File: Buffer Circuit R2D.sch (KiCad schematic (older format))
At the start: 25 parts, among them Q13 BC846B, Q14 BC856B, Q15 BC846B, Q16 BC856B, U10 AD8664ARZ

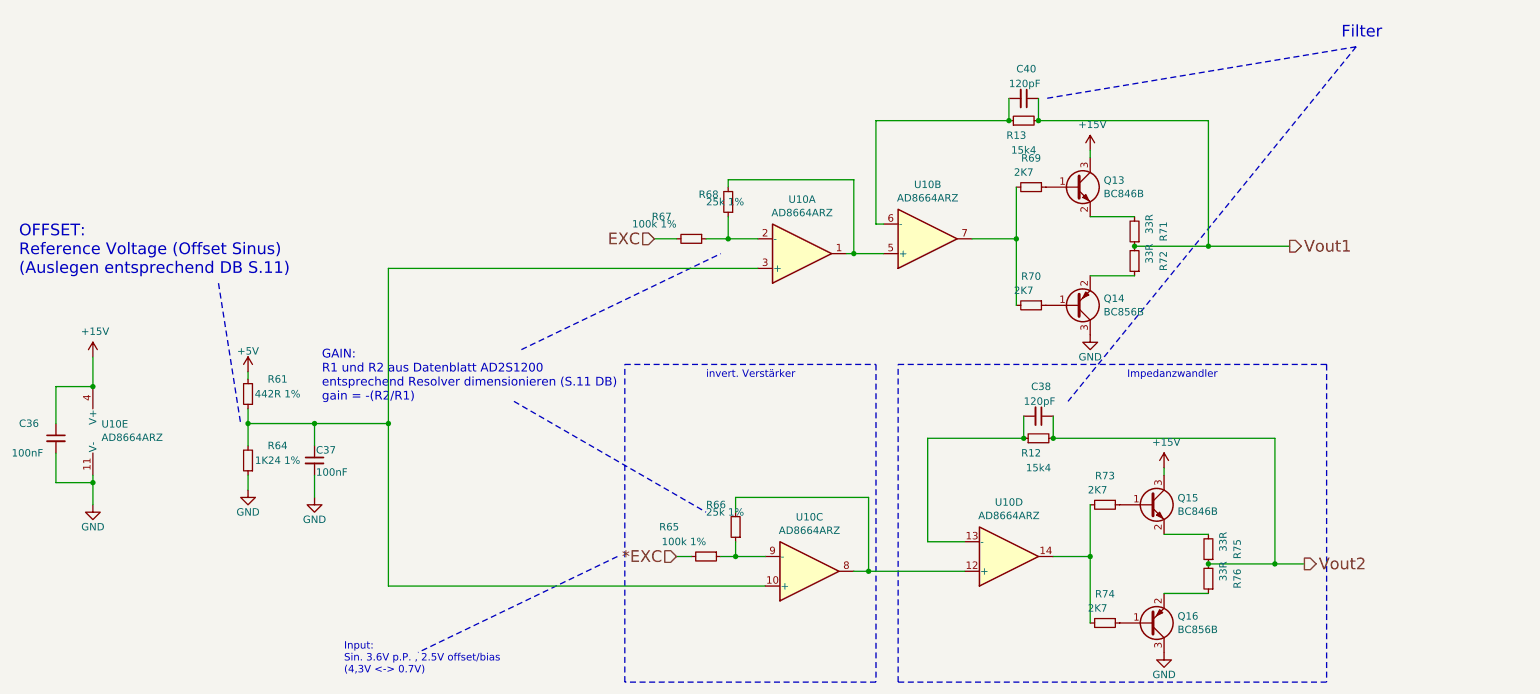
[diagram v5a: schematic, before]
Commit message: -changed ad2s1200 to ad2s1205  (pin compatibel) -changed excitation-buffer circuit. (AD8397 in use now) -fixed thermal-connections of planes
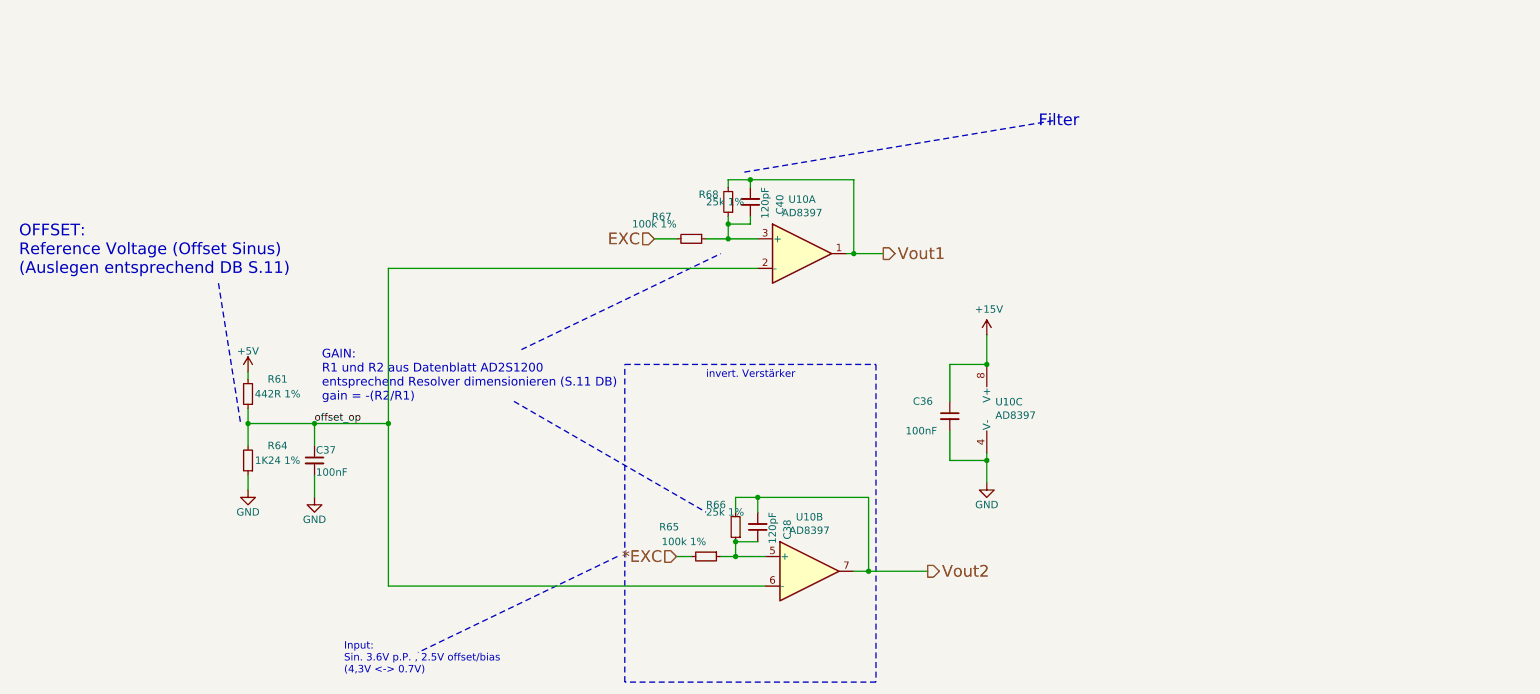
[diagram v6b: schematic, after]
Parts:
- removed Q13, Q15: BC846B, Package_TO_SOT_SMD:SOT-23, symbol Transistor_BJT:BC847
- removed Q14, Q16: BC856B, Package_TO_SOT_SMD:SOT-23, symbol Amalga_100-rescue:Q_PNP_BEC-Device
- removed R12, R13: 15k4, Resistor_SMD:R_0805_2012Metric, symbol Amalga_100-rescue:R_Small-Device
- removed R69, R70, R73, R74: 2K7, Resistor_SMD:R_0805_2012Metric, symbol Amalga_100-rescue:R_Small-Device
- removed R71, R72, R75, R76: 33R, Resistor_SMD:R_0805_2012Metric, symbol Amalga_100-rescue:R_Small-Device
- removed U10: AD8664ARZ, Housings_SOIC:SOIC-14_3.9x8.7mm_Pitch1.27mm, symbol Amplifier_Operational:OPA1604
- added U10: AD8397, Package_SO:SOIC-8_3.9x4.9mm_P1.27mm, symbol Amplifier_Operational:AD8620
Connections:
- net +15V: now also U10.8 (V+)
- net GND: now also U10.4 (V-)
- net Vout1: now also C40.2, R68.2, U10.1; no longer C40.1
- net Vout2: now also C38.2, R66.2, U10.7; no longer C38.1
- net offset_op: now reaches C37.1, R61.1, R64.2
- net offset_op: now also U10.2 (-), U10.6 (-)
- net at R67.1, R68.1: now also C40.1, U10.3 (+)
- net at R65.1, R66.1: now also C38.1, U10.5 (+)
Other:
- note removed: "Impedanzwandler"
- moved on the sheet: C36, C38, C40

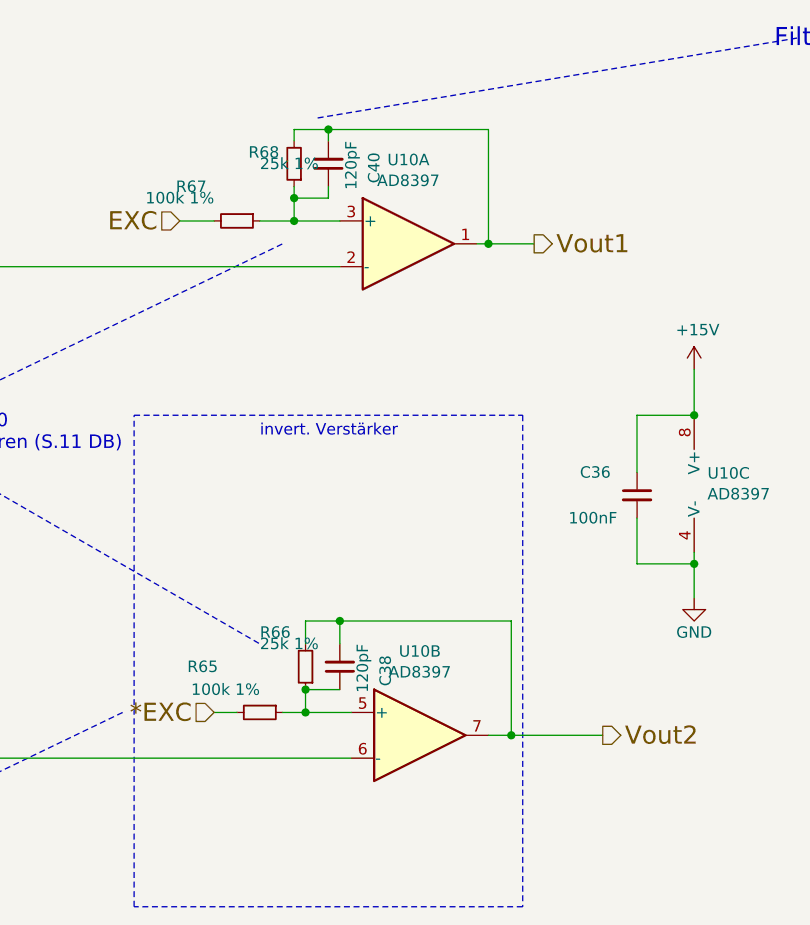
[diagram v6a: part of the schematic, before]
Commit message: -fixed wrong connection on +/- of opamp in exc-buffer
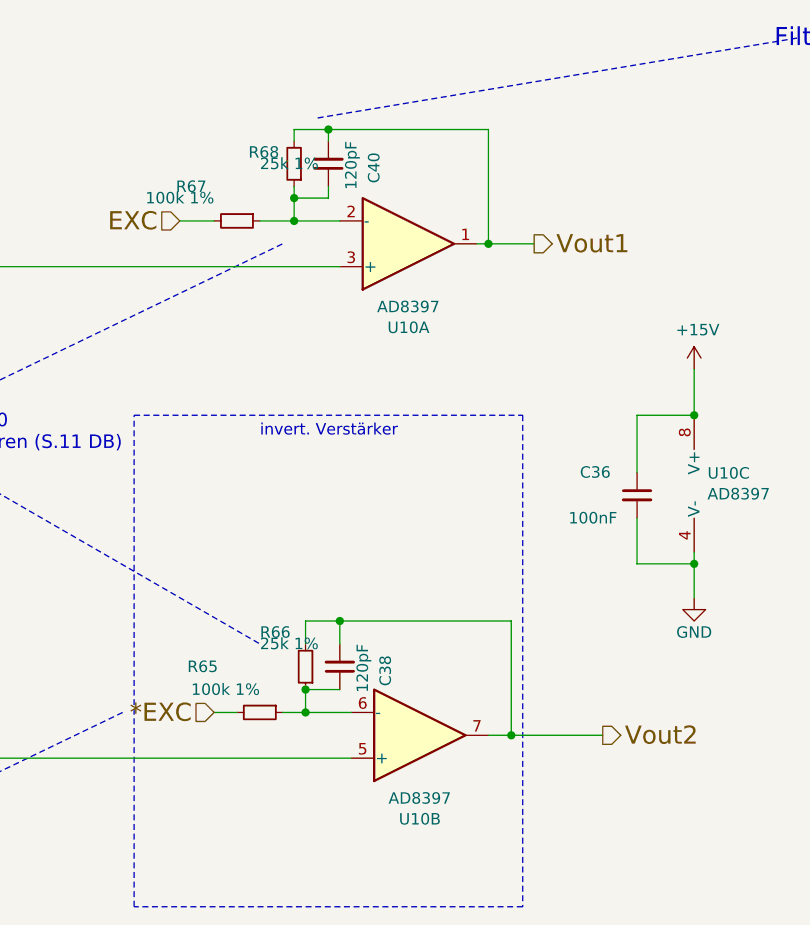
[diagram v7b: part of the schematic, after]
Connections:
- net offset_op: now also U10.3 (+), U10.5 (+); no longer U10.2 (-), U10.6 (-)
- net at C38.1, R65.1, R66.1: now also U10.6 (-); no longer U10.5 (+)
- net at C40.1, R67.1, R68.1: now also U10.2 (-); no longer U10.3 (+)
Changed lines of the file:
@@
 F 3 "https://www.analog.com/media/en/technical-documentation/data-sheets/AD8610_8620.pdf" H 5850 2450 50  0001 C CNN
 	1    5850 2450
-	1    0    0    -1
+	1    0    0    1
 $EndComp
 $Comp
@@
 F 3 "https://www.analog.com/media/en/technical-documentation/data-sheets/AD8610_8620.pdf" H 5900 4600 50  0001 C CNN
 	2    5900 4600
-	1    0    0    -1
+	1    0    0    1
 $EndComp
 $Comp
